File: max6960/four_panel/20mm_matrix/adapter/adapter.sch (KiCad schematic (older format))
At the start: 6 parts, among them M1 BETLUX-LED-8X8_C, M2 BETLUX-LED-8X8_C, M3 BETLUX-LED-8X8_C, M4 BETLUX-LED-8X8_C, P1 LED-MATRIX-2X-8X8-FEMALE, P2 LED-MATRIX-2X-8X8-FEMALE

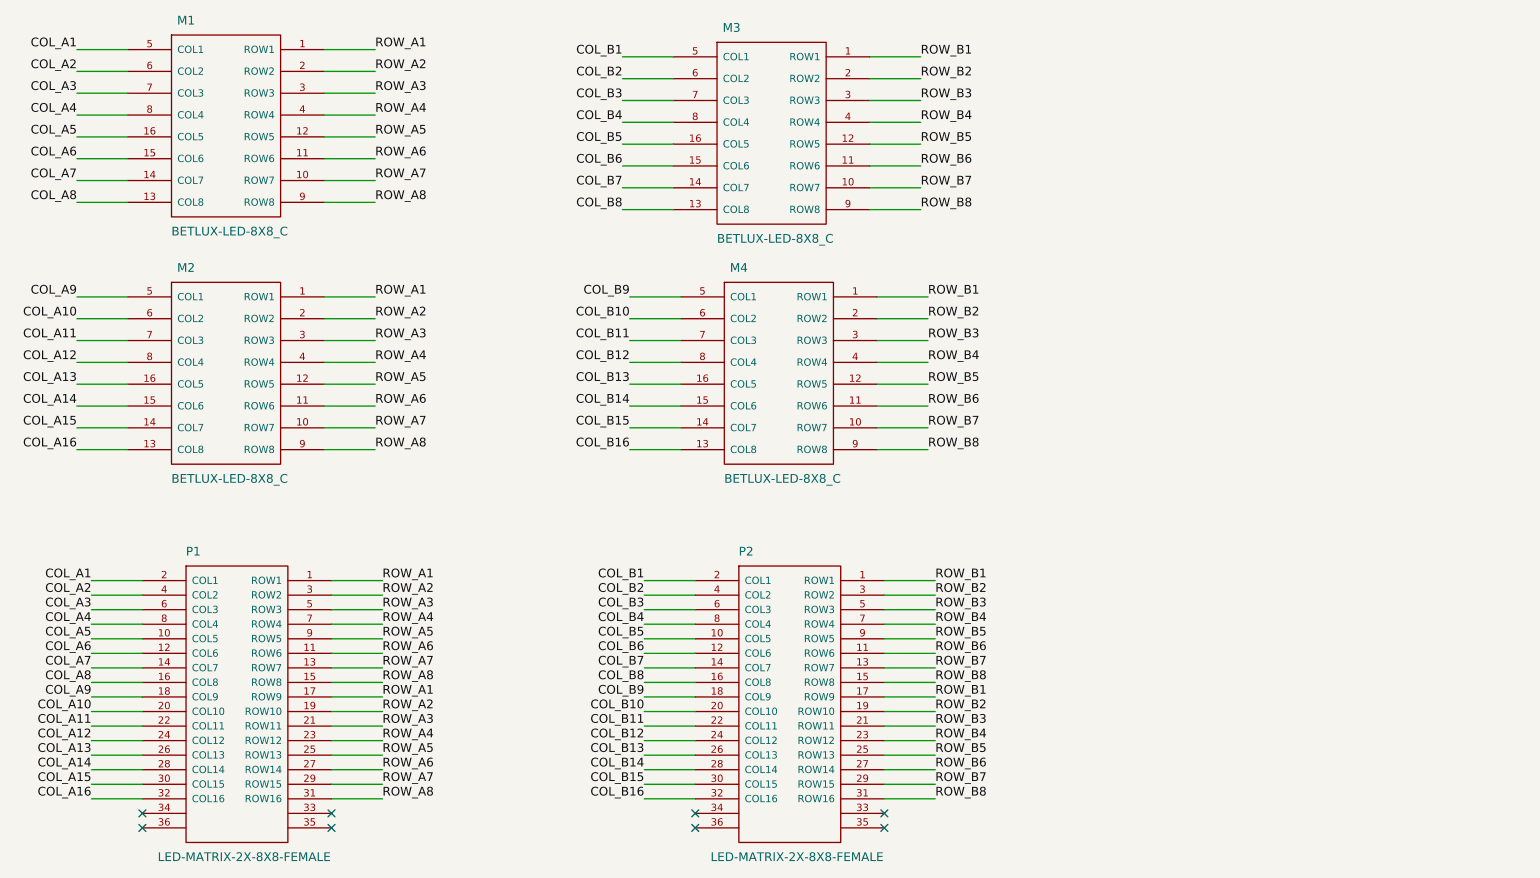
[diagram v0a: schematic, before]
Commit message: Re-routed four matrix panel driver and adapter. Switched to board-to-board connectors from major league.
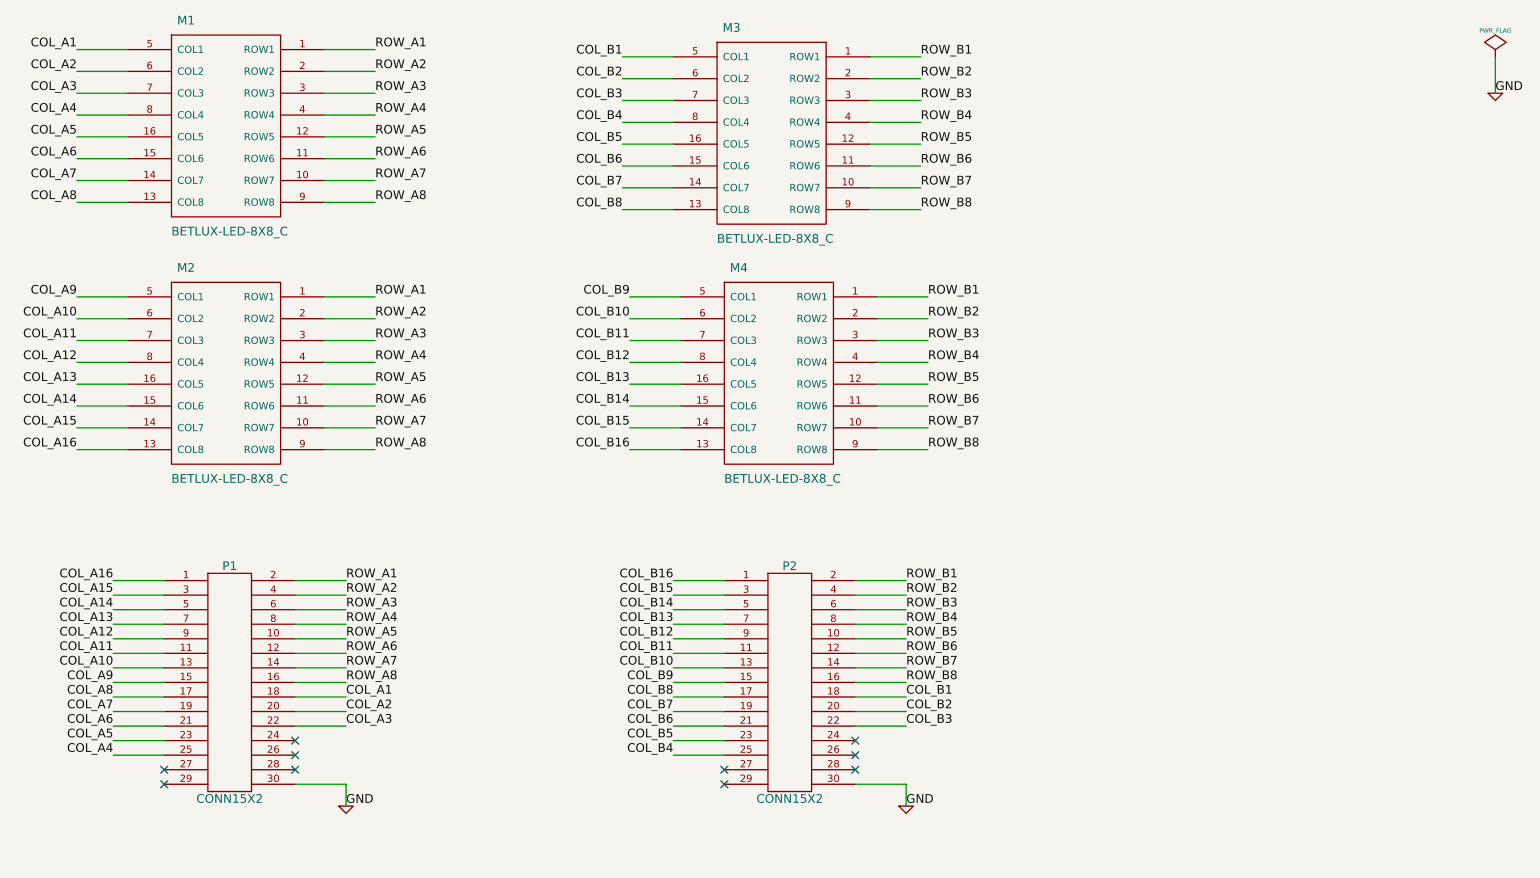
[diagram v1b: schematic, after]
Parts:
- removed P1, P2: LED-MATRIX-2X-8X8-FEMALE, symbol LED-MATRIX-2X-8X8-FEMALE
- added P1, P2: CONN15X2, symbol CONN15X2
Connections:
- net COL_A1: now also P1.18
- net COL_A10: now also P1.13
- net COL_A11: now also P1.11
- net COL_A12: now also P1.9
- net COL_A13: now also P1.7
- net COL_A14: now also P1.5
- net COL_A15: now also P1.3
- net COL_A16: now also P1.1
- net COL_A2: now also P1.20
- net COL_A3: now also P1.22
- net COL_A4: now also P1.25
- net COL_A5: now also P1.23
- net COL_A6: now also P1.21
- net COL_A7: now also P1.19
- net COL_A8: now also P1.17
- net COL_A9: now also P1.15
- net COL_B1: now also P2.18
- net COL_B10: now also P2.13
- net COL_B11: now also P2.11
- net COL_B12: now also P2.9
- net COL_B13: now also P2.7
- net COL_B14: now also P2.5
- net COL_B15: now also P2.3
- net COL_B16: now also P2.1
- net COL_B2: now also P2.20
- net COL_B3: now also P2.22
- net COL_B4: now also P2.25
- net COL_B5: now also P2.23
- net COL_B6: now also P2.21
- net COL_B7: now also P2.19
- net COL_B8: now also P2.17
- net COL_B9: now also P2.15
- net ROW_A1: now also P1.2
- net ROW_A2: now also P1.4
- net ROW_A3: now also P1.6
- net ROW_A4: now also P1.8
- net ROW_A5: now also P1.10
- net ROW_A6: now also P1.12
- net ROW_A7: now also P1.14
- net ROW_A8: now also P1.16
- net ROW_B1: now also P2.2
- net ROW_B2: now also P2.4
- net ROW_B3: now also P2.6
- net ROW_B4: now also P2.8
- net ROW_B5: now also P2.10
- net ROW_B6: now also P2.12
- net ROW_B7: now also P2.14
- net ROW_B8: now also P2.16
- new net GND: P1.30, P2.30
- no-connect marks 8 -> 10
